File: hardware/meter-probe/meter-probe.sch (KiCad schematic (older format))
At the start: 17 parts, among them J1 Main Board, Q1 BSS138, SW1 Sensor Button, U1 RT9193, U2 TCS3472, U3 P82B96

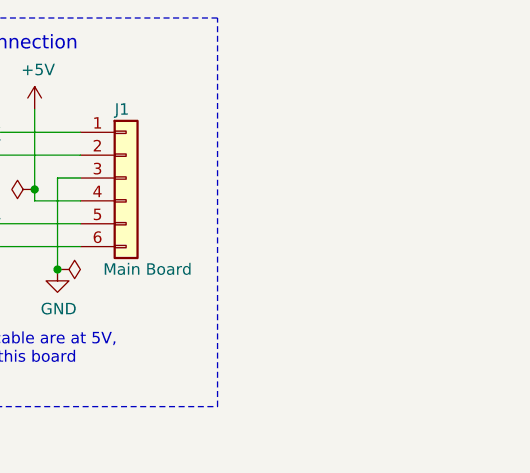
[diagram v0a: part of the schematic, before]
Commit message: Meter Probe (Rev A) as ordered from fab
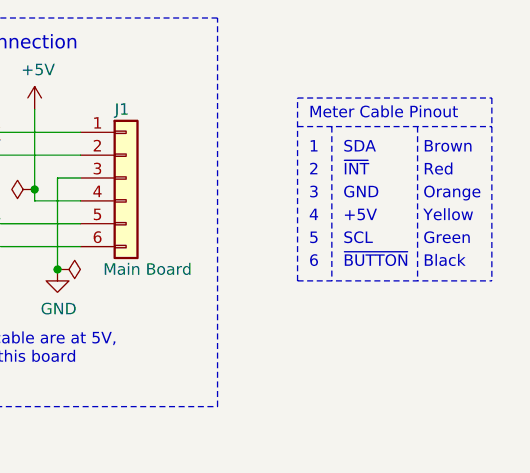
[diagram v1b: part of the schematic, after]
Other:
- note added: "+5V"
- note added: "1"
- note added: "2"
- note added: "3"
- note added: "4"
- note added: "5"
- note added: "6"
- note added: "Black"
- note added: "Brown"
- note added: "GND"
- note added: "Green"
- note added: "Meter Cable Pinout"
- note added: "Orange"
- note added: "Red"
- note added: "SCL"
- note added: "SDA"
- note added: "Yellow"
- note added: "~BUTTON"
- note added: "~INT"
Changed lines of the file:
@@
 Sheet 1 1
 Title "Printalyzer - Meter Probe"
-Date "2020-10-23"
+Date "2020-10-28"
 Rev "A"
 Comp "LogicProbe.org"
@@
 Wire Wire Line
 	5400 1450 5400 1500
+Text Notes 7850 1450 0    50   ~ 0
+Brown
+Text Notes 7850 1550 0    50   ~ 0
+Red
+Text Notes 7850 1650 0    50   ~ 0
+Orange
+Text Notes 7850 1750 0    50   ~ 0
+Yellow
+Text Notes 7850 1850 0    50   ~ 0
+Green
+Text Notes 7850 1950 0    50   ~ 0
+Black
+Text Notes 7350 1450 0    50   ~ 0
+1
+Text Notes 7350 1550 0    50   ~ 0
+2
+Text Notes 7350 1650 0    50   ~ 0
+3
+Text Notes 7350 1750 0    50   ~ 0
+4
+Text Notes 7350 1850 0    50   ~ 0
+5
+Text Notes 7350 1950 0    50   ~ 0
+6
+Text Notes 7500 1450 0    50   ~ 0
+SDA
+Text Notes 7500 1550 0    50   ~ 0
+~INT
+Text Notes 7500 1650 0    50   ~ 0
+GND
+Text Notes 7500 1750 0    50   ~ 0
++5V
+Text Notes 7500 1850 0    50   ~ 0
+SCL
+Text Notes 7500 1950 0    50   ~ 0
+~BUTTON
+Text Notes 7350 1300 0    50   ~ 0
+Meter Cable Pinout
+Wire Notes Line style solid
+	7450 1325 7450 2000
+Wire Notes Line style solid
+	7300 2000 7300 1200
+Wire Notes Line style solid
+	7300 1200 8150 1200
+Wire Notes Line style solid
+	8150 1200 8150 2000
+Wire Notes Line style solid
+	7300 2000 8150 2000
+Wire Notes Line style solid
+	7300 1325 8150 1325
+Wire Notes Line style solid
+	7825 1325 7825 2000
 $EndSCHEMATC
